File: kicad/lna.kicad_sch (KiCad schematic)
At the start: 35 parts, among them J4 Conn_01x02_Pin, J5 Conn_Coaxial_Small, J6 Conn_Coaxial_Small, U5 L78L05_SOT89, U6 BFP640, U7 BFP640, U8 BFP640

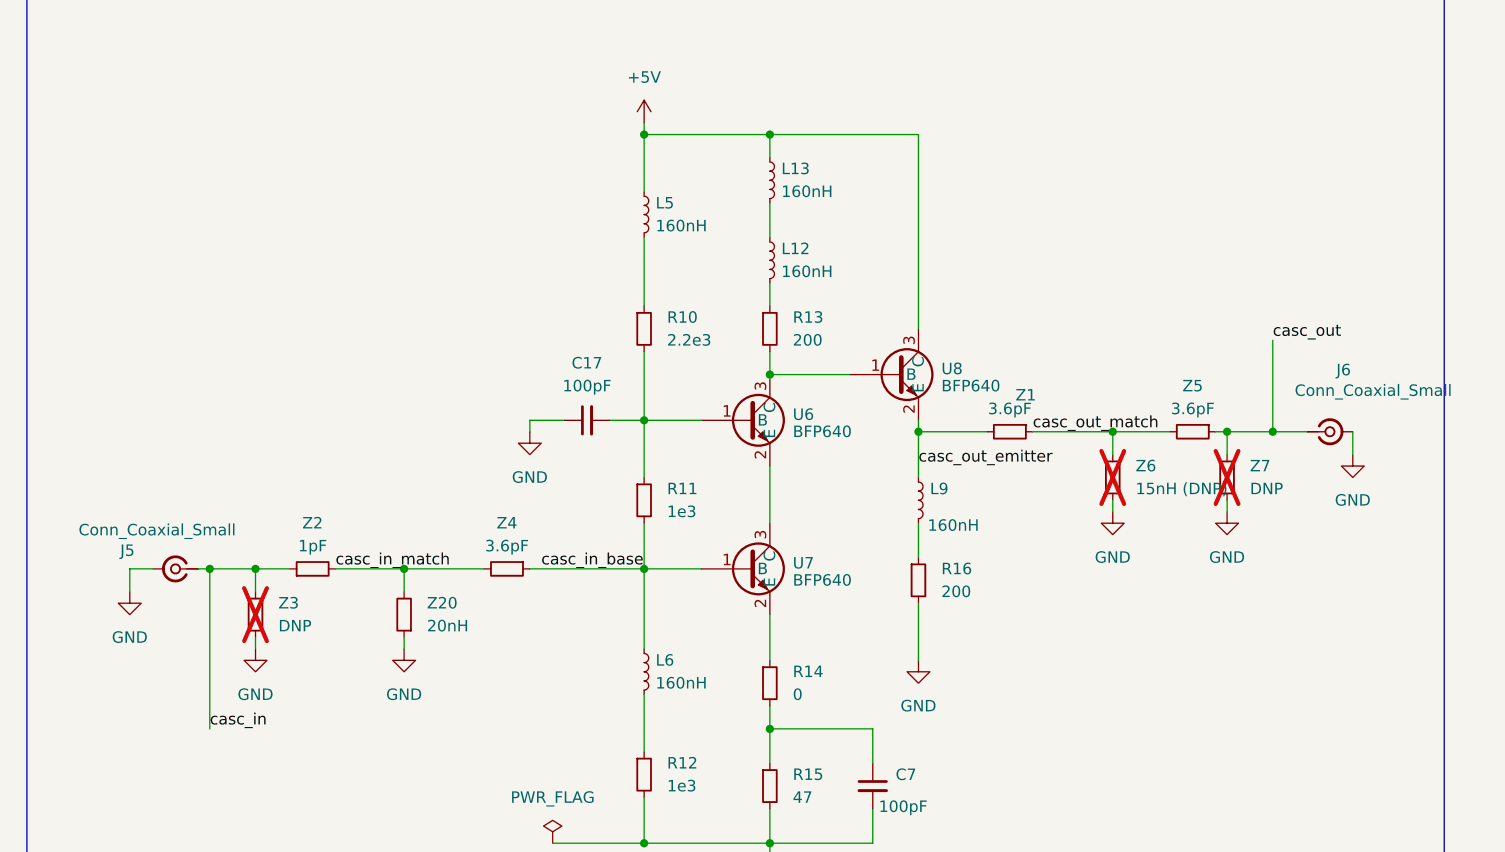
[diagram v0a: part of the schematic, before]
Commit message: [kicad] Update to kicad 9
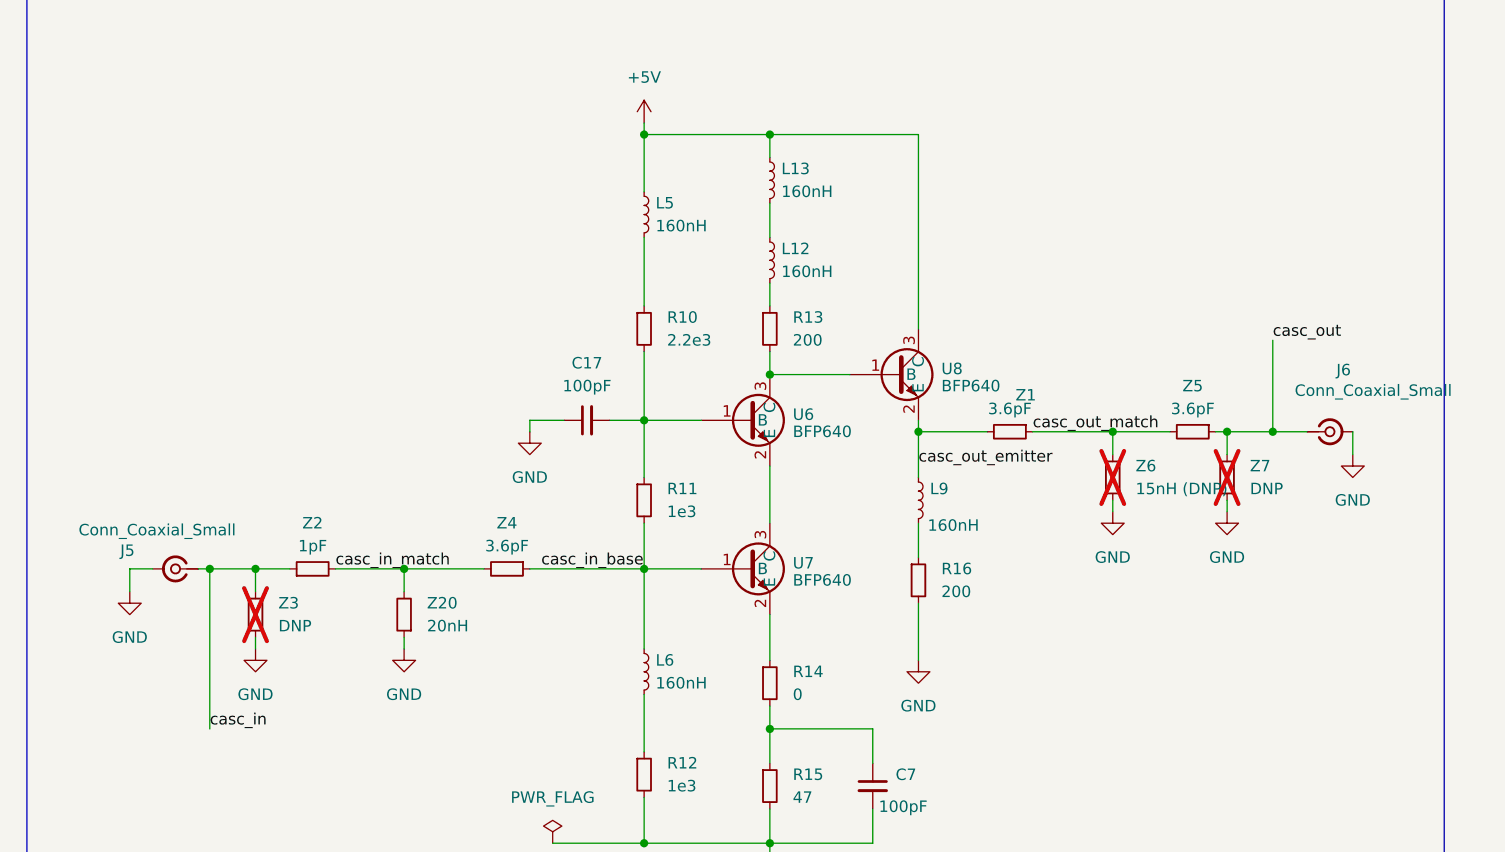
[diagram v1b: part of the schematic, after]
